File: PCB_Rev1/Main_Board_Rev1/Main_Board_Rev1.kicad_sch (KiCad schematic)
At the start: 2 parts, among them J1 Raspberry_Pi_2_3

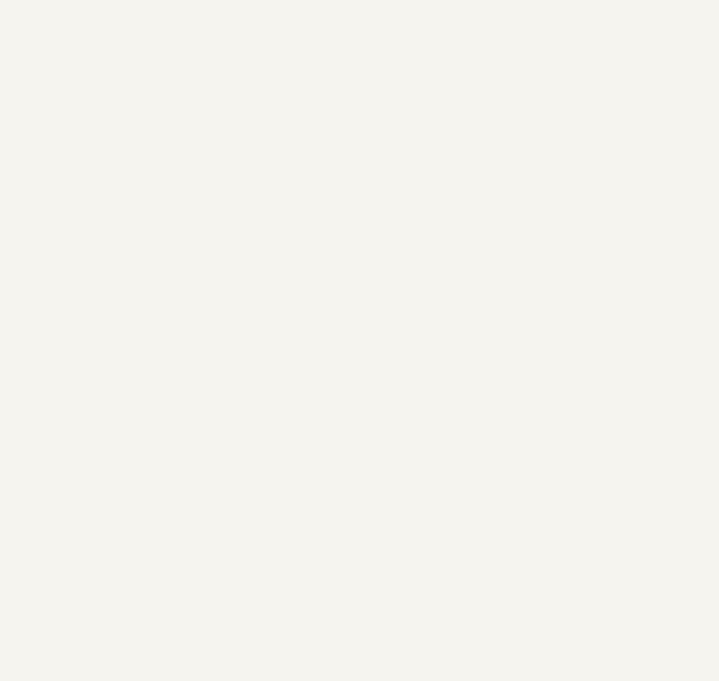
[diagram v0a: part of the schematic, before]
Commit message: Audio subsystem re-created
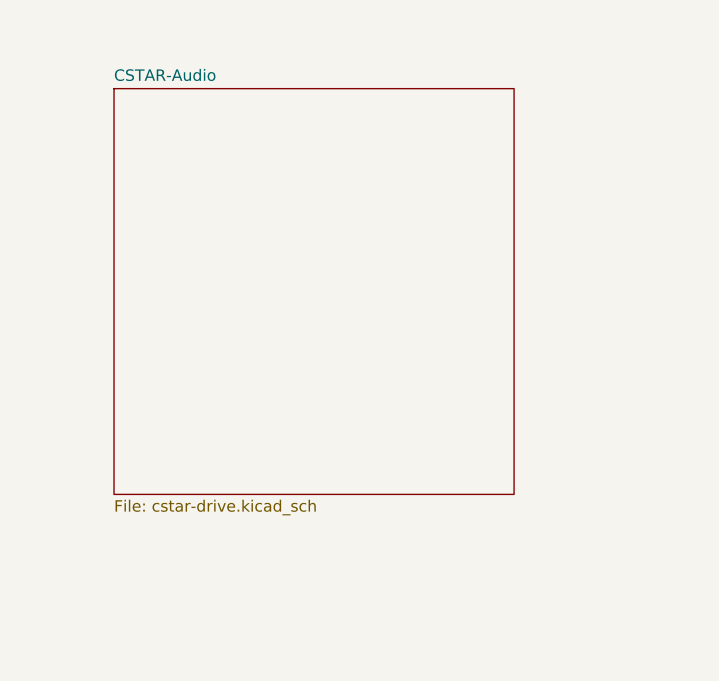
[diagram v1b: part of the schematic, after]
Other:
- added sheet CSTAR-Audio (cstar-drive.kicad_sch)
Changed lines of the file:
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@@
+		)
+	)
+	(sheet
+		(at 27.94 35.56)
+		(size 44.45 45.085)
+		(fields_autoplaced yes)
+		(stroke
+			(width 0.1524)
+			(type solid)
+		)
+		(fill
+			(color 0 0 0 0.0000)
+		)
+		(property "Sheetname" "CSTAR-Audio"
+			(at 27.94 34.8484 0)
+			(effects
+				(font
+					(size 1.27 1.27)
+				)
+				(justify left bottom)
+			)
+		)
+		(property "Sheetfile" "cstar-drive.kicad_sch"
+			(at 27.94 81.2296 0)
+			(effects
+				(font
+					(size 1.27 1.27)
+				)
+				(justify left top)
+			)
+		)
+		(instances
+			(project "Main_Board_Rev1"
+				(path "/8f5a23de-a1fa-4202-92fb-c2ac3de0338c"
+					(page "4")
+				)
+			)
 		)
 	)

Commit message: Revert "Audio subsystem re-created"
This reverts commit 6dc47edf88eae56b01440ce5f2dfd5da155ce597.
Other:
- removed sheet CSTAR-Audio
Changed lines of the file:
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@@
-		)
-	)
-	(sheet
-		(at 27.94 35.56)
-		(size 44.45 45.085)
-		(fields_autoplaced yes)
-		(stroke
-			(width 0.1524)
-			(type solid)
-		)
-		(fill
-			(color 0 0 0 0.0000)
-		)
-		(property "Sheetname" "CSTAR-Audio"
-			(at 27.94 34.8484 0)
-			(effects
-				(font
-					(size 1.27 1.27)
-				)
-				(justify left bottom)
-			)
-		)
-		(property "Sheetfile" "cstar-drive.kicad_sch"
-			(at 27.94 81.2296 0)
-			(effects
-				(font
-					(size 1.27 1.27)
-				)
-				(justify left top)
-			)
-		)
-		(instances
-			(project "Main_Board_Rev1"
-				(path "/8f5a23de-a1fa-4202-92fb-c2ac3de0338c"
-					(page "4")
-				)
-			)
 		)
 	)
